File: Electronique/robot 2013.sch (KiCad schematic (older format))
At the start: 7 parts

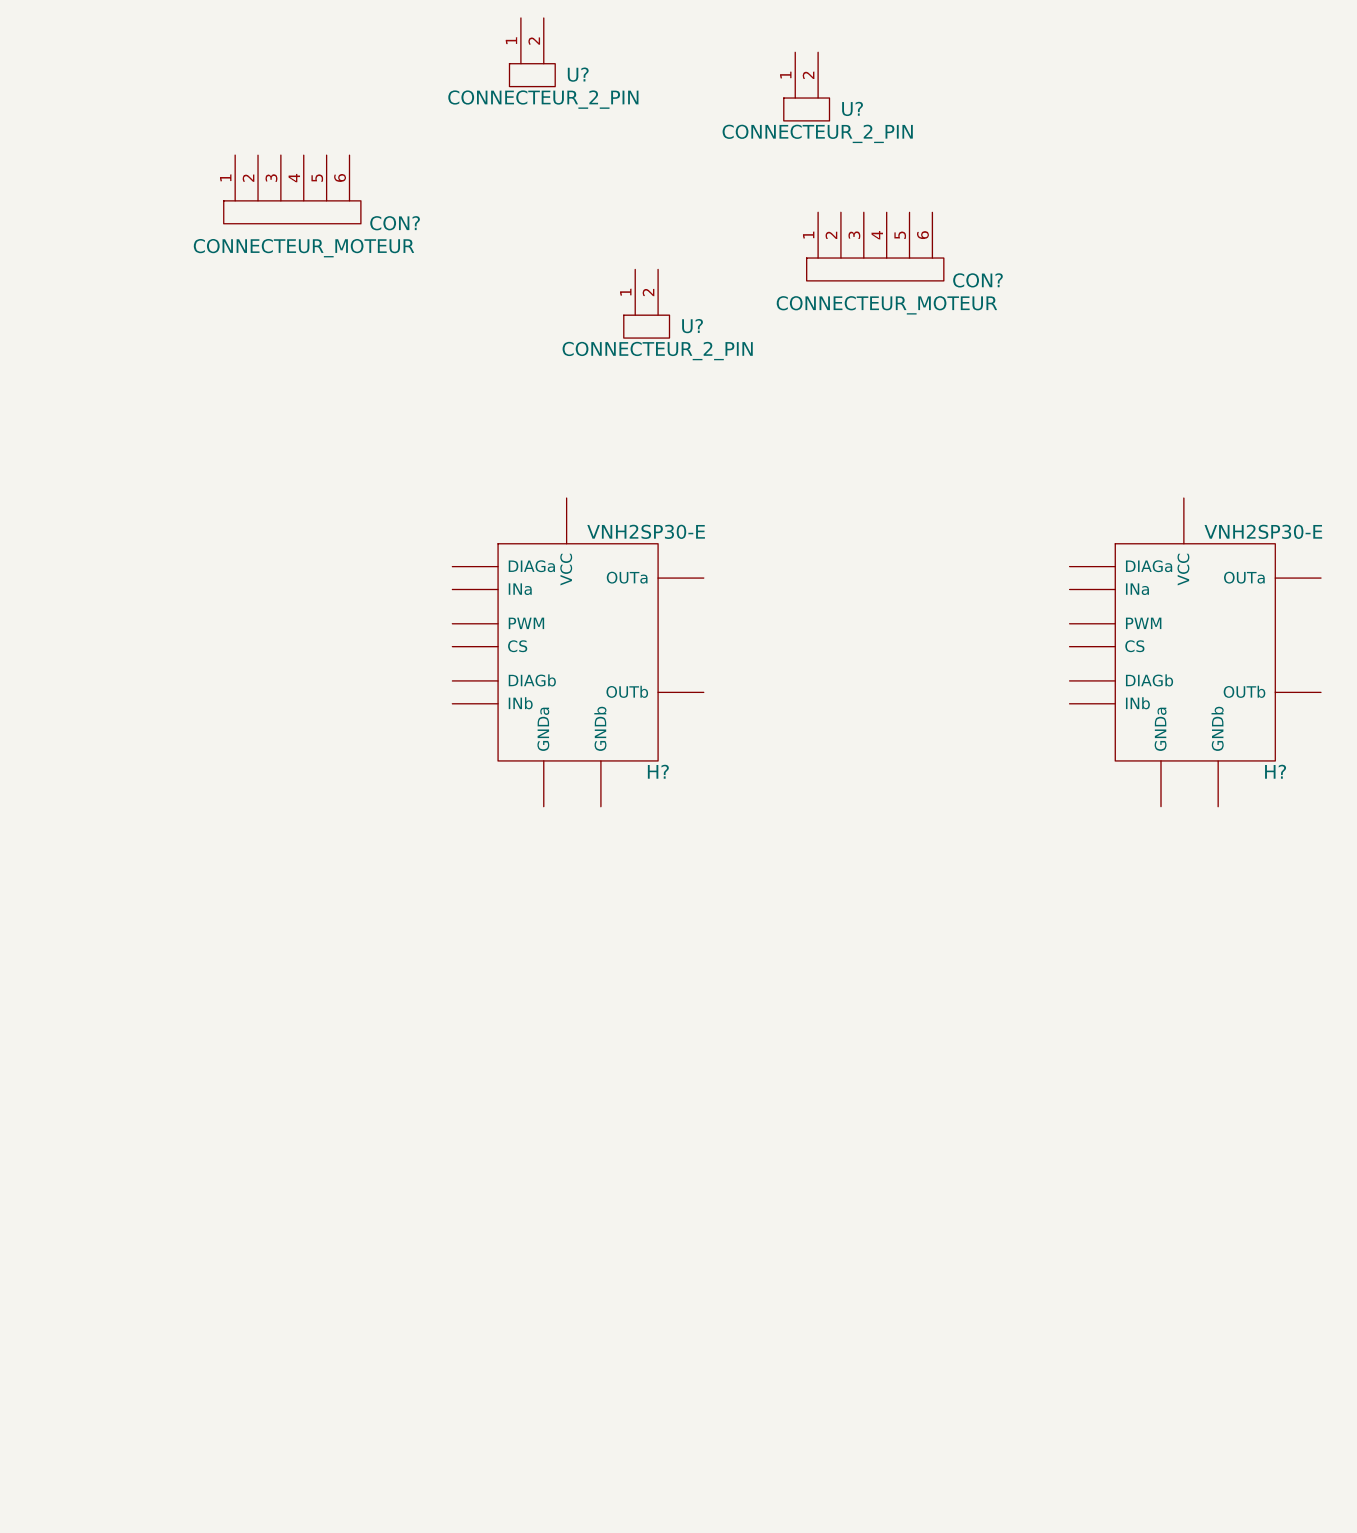
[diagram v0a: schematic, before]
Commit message: Electronique, Ajout du schématique de la carte LPCXpresso dans la librairie test de KiCad
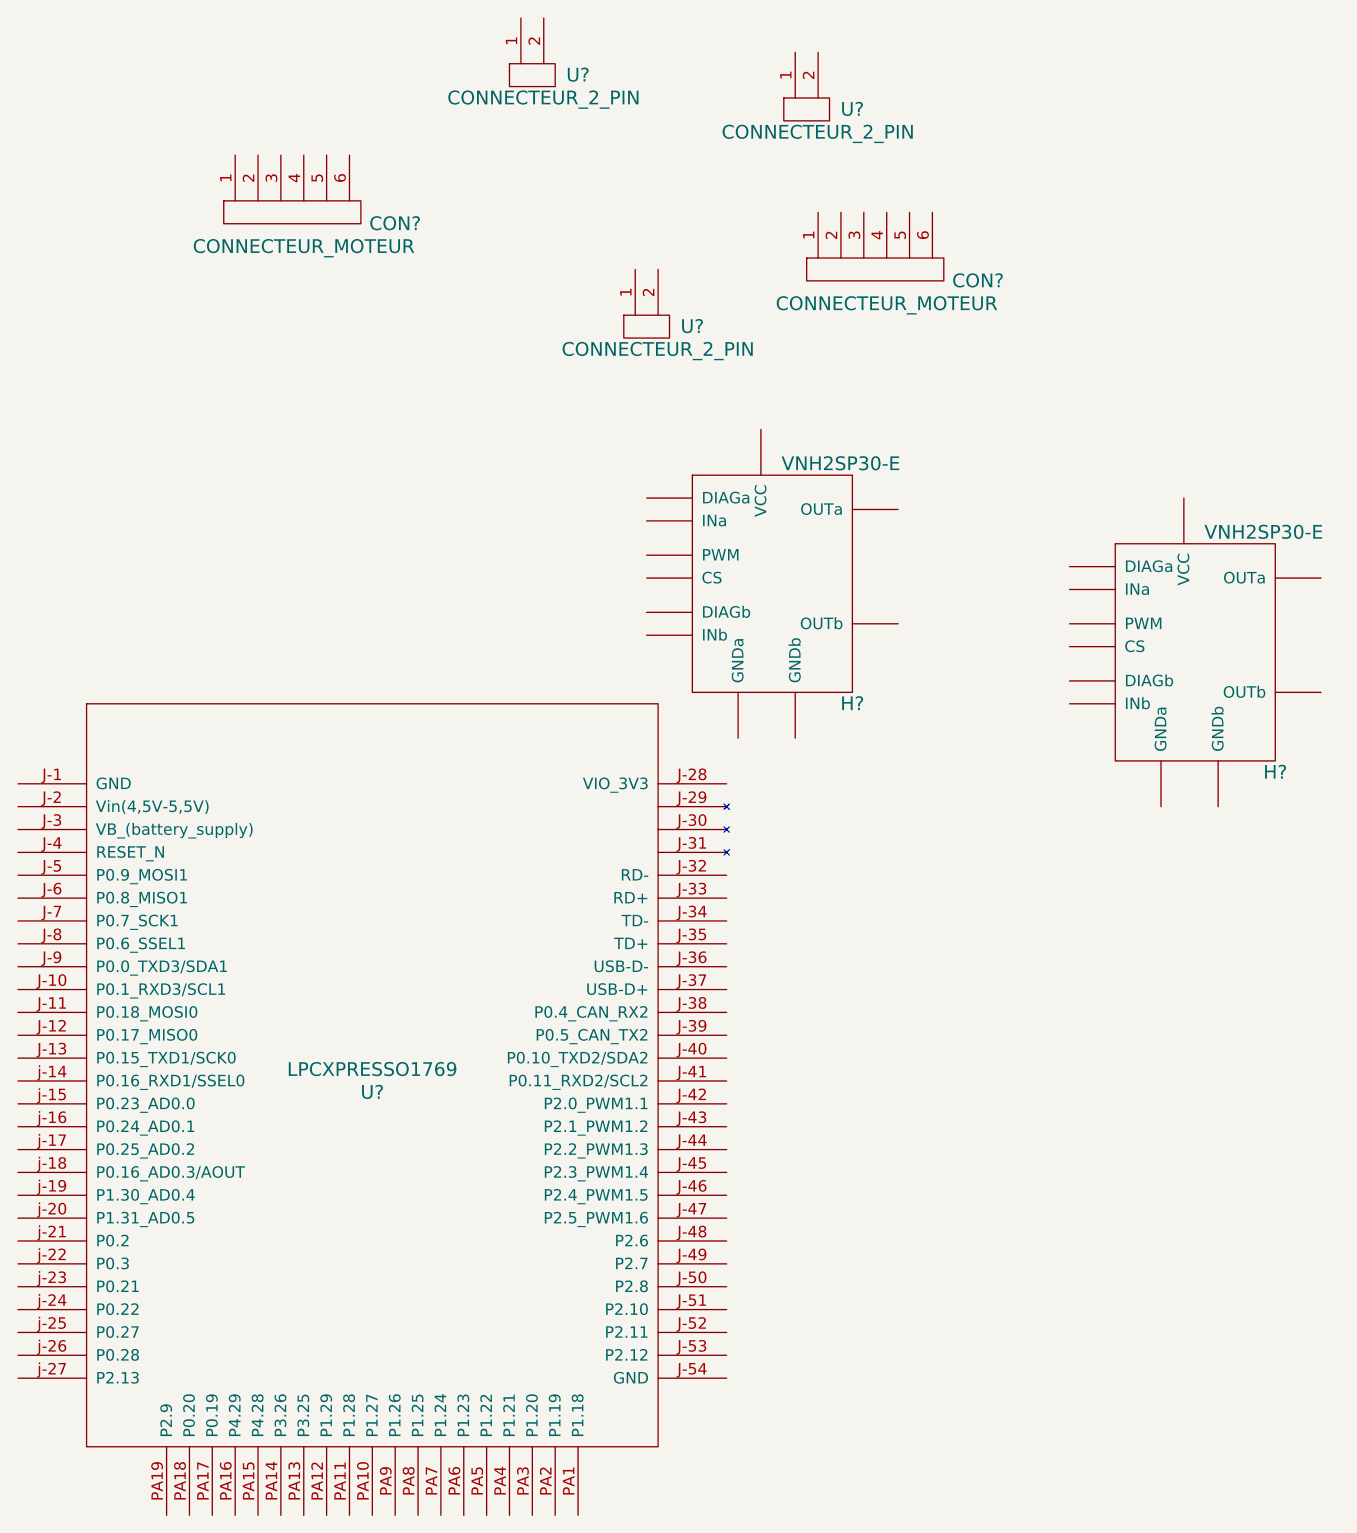
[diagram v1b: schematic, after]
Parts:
- added U?: LPCXPRESSO1769, symbol LPCXPRESSO1769
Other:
- moved on the sheet: H?
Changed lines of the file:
@@
-EESchema Schematic File Version 2  date 23/06/2012 17:31:21
+EESchema Schematic File Version 2  date jeu. 02 août 2012 18:06:57 CEST
 LIBS:power
 LIBS:device
@@
 EELAYER 25  0
 EELAYER END
-$Descr A4 11700 8267
+$Descr A4 11693 8268
 encoding utf-8
 Sheet 1 1
 Title ""
-Date "23 jun 2012"
+Date "2 aug 2012"
 Rev ""
 Comp ""
@@
 L VNH2SP30-E H?
 U 1 1 4FE5C95F
-P 4150 3400
-F 0 "H?" H 4500 2850 60  0000 C CNN
-F 1 "VNH2SP30-E" H 4450 3900 60  0000 C CNN
-	1    4150 3400
+P 5000 3100
+F 0 "H?" H 5350 2550 60  0000 C CNN
+F 1 "VNH2SP30-E" H 5300 3600 60  0000 C CNN
+	1    5000 3100
 	1    0    0    -1
 $EndComp
+$Comp
+L LPCXPRESSO1769 U?
+U 1 1 501AD567
+P 3250 5300
+F 0 "U?" H 3250 5250 60  0000 C CNN
+F 1 "LPCXPRESSO1769" H 3250 5350 60  0000 C CNN
+	1    3250 5300
+	1    0    0    -1
+$EndComp
